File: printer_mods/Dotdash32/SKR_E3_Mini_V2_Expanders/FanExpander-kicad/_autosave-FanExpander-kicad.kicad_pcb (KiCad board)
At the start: 2 copper layers, 96.8 x 21.3 mm, 66 parts, among them J0 FAN0, J1 FAN1, J10 FAN0_IN, J11 HI_PWR_Inputs, J2 FAN2, J3 FAN3, J4 FAN4, J5 FAN5, J6 FAN6, J7 FAN7, J8 EXP1_IN, J9 5V_In, Q1 IRLML6344, Q2 IRLML6344, Q3 IRLML6344, Q4 IRLML6344, Q5 IRLML6344, Q6 IRLML6344, Q7 IRLML6344

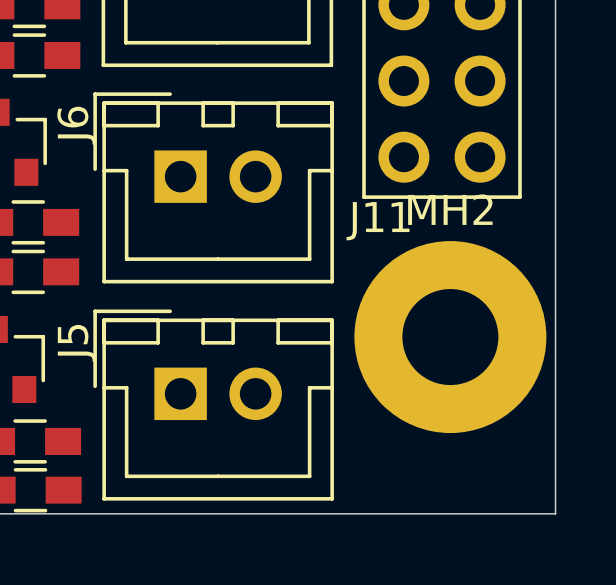
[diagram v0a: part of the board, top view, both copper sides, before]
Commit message: feat: breakaway layout, using 1mm spacing headers
it works, but its SOOO LOOOONG, going to try again and make it
more compact so I don't feel bad about this long stick in my printer
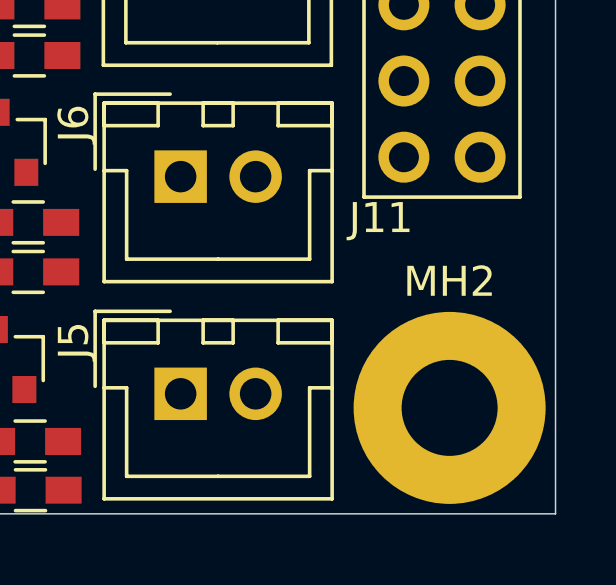
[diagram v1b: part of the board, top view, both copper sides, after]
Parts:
- moved MH2 2.36 mm to (132.9, 57.9)
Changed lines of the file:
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@@
   )
   (module Mounting_Holes:MountingHole_3.2mm_M3_Pad (layer F.Cu)
-    (at 132.8928 55.5244)
+    (at 132.8674 57.8866)
     (descr "Mounting Hole 3.2mm, M3")
     (tags "mounting hole 3.2mm m3")
